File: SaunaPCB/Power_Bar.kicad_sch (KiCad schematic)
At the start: 37 parts, among them J200a1 KL2RM7.62, J200b1 KL3RM7.62, J201a1 KL2RM7.62, J201b1 KL3RM7.62, J202 KL3RM7.62, J203 KL2RM7.62, K200 Relais_SPDT_CO, K201 Relais_SPDT_CO, K202 Relais_SPDT_CO, K203 Relais_SPDT_CO, K204 Relais_SPDT_CO, K205 Relais_SPDT_CO, K206 Relais_SPDT_CO, U1 4N25, U2 4N25, U3 4N25

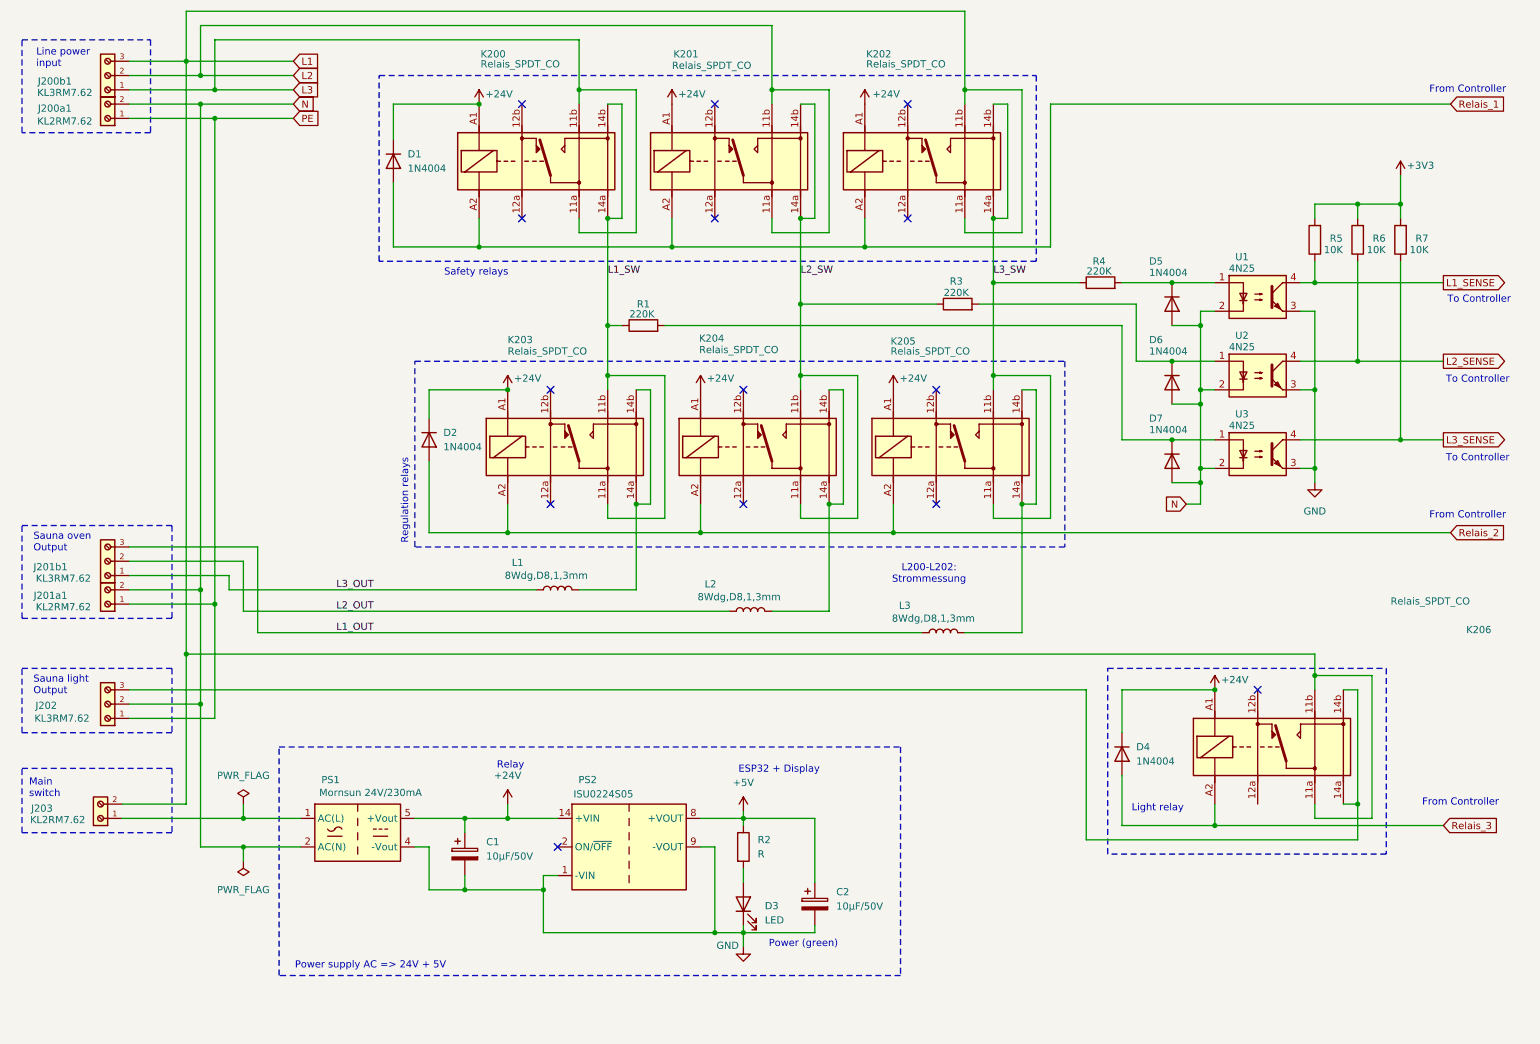
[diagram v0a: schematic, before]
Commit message: Working on schematic and PCB -AC/DC and DC/DC converters with correct symbol and footprint now - rough placement of the power parts
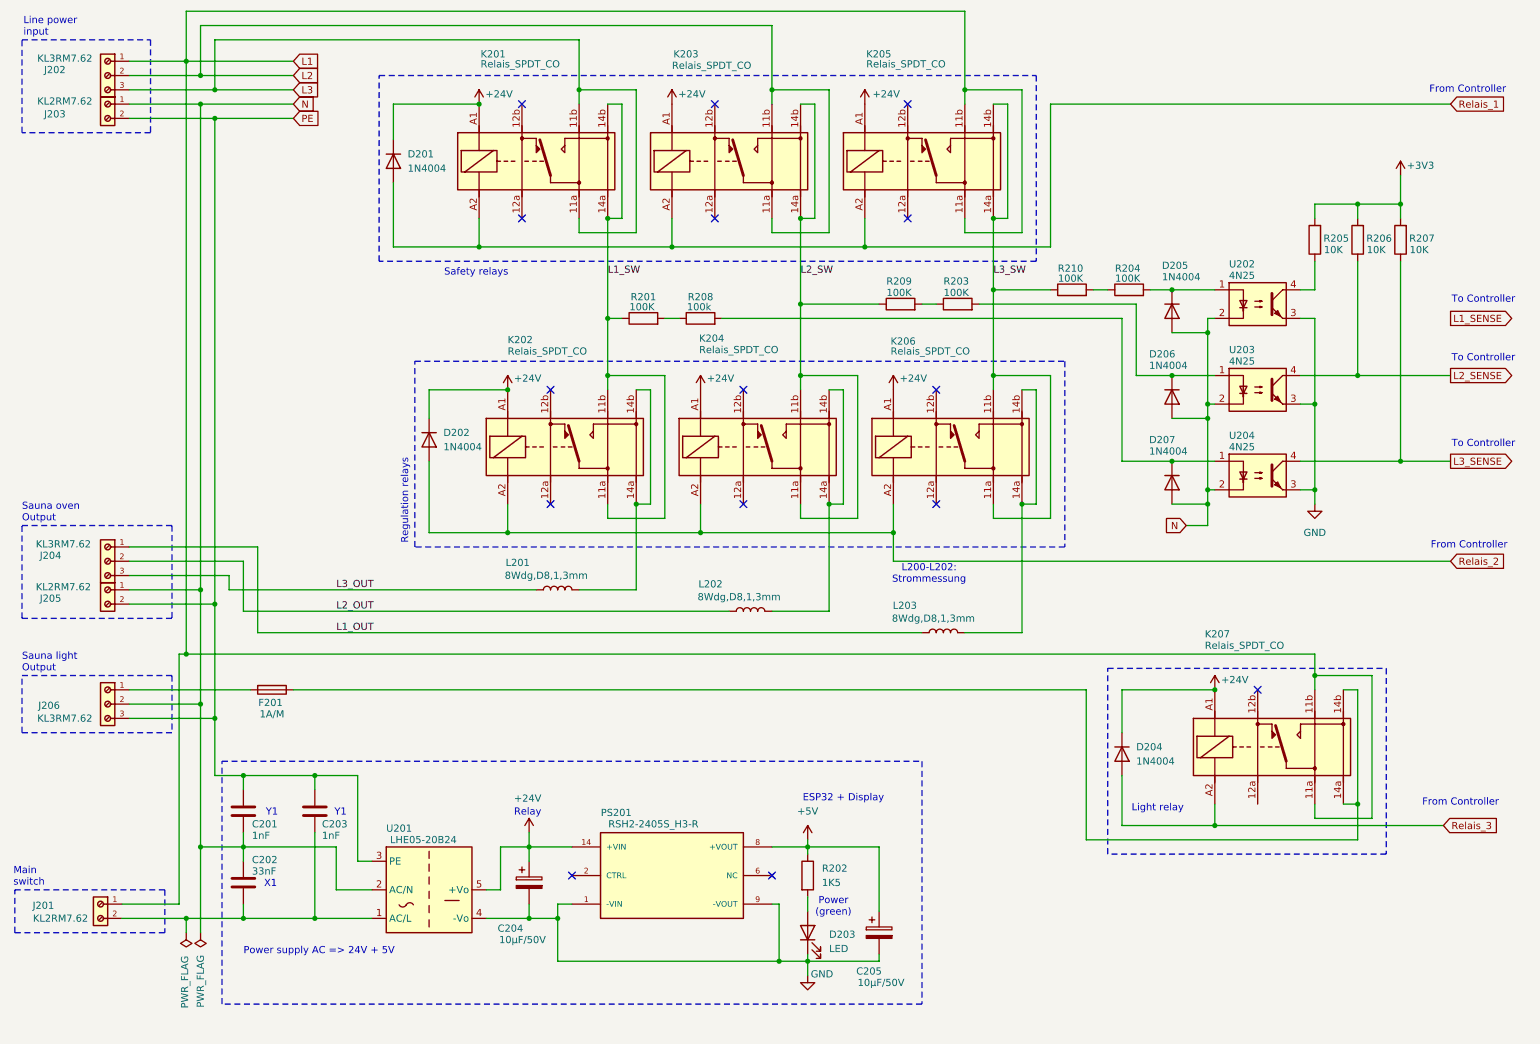
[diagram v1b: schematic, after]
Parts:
- removed PS1: Mornsun 24V/230mA, Converter_ACDC:Converter_ACDC_RECOM_RAC05-xxSK_THT, symbol Converter_ACDC:RAC05-24SK
- removed PS2: ISU0224S05, Converter_DCDC:Converter_DCDC_XP_POWER-ISU02_SMD, symbol Converter_DCDC:ISU0224S05
- added C201, C203: 1nF, Capacitor_THT:C_Axial_L12.0mm_D6.5mm_P15.00mm_Horizontal, symbol Device:C
- added C202: 33nF, Capacitor_THT:C_Axial_L12.0mm_D6.5mm_P15.00mm_Horizontal, symbol Device:C
- added F201: 1A/M, Fuse:Fuseholder_Cylinder-5x20mm_Schurter_0031_8201_Horizontal_Open, symbol Device:Fuse
- added PS201: RSH2-2405S_H3-R, DCDC:CONV_RSH2-2405S_H3-R, symbol DC-DC:RSH2-2405S_H3-R
- added R208: 100k, Resistor_SMD:R_1206_3216Metric, symbol Device:R
- added R209, R210: 100K, Resistor_SMD:R_1206_3216Metric, symbol Device:R
- added U201: LHE05-20B24, Mornsun_ACDC:LHE05-20B24, symbol Project:Mornsun_AC_DC
- D205: renamed from D5; footprint Diode_THT:D_DO-41_SOD81_P10.16mm_Horizontal -> Diode_SMD:D_SMA_Handsoldering
- D206: renamed from D6; footprint Diode_THT:D_DO-41_SOD81_P10.16mm_Horizontal -> Diode_SMD:D_SMA_Handsoldering
- D207: renamed from D7; footprint Diode_THT:D_DO-41_SOD81_P10.16mm_Horizontal -> Diode_SMD:D_SMA_Handsoldering
- L201: renamed from L1; footprint Inductor_THT:L_Toroid_Vertical_L13.0mm_W6.5mm_P5.60mm -> SaunaProject:Current_Coil_15X14
- L202: renamed from L2; footprint Inductor_THT:L_Toroid_Vertical_L13.0mm_W6.5mm_P5.60mm -> SaunaProject:Current_Coil_15X14
- L203: renamed from L3; footprint Inductor_THT:L_Toroid_Vertical_L13.0mm_W6.5mm_P5.60mm -> SaunaProject:Current_Coil_15X14
- R201: renamed from R1; value 220K -> 100K; footprint Resistor_THT:R_Axial_DIN0207_L6.3mm_D2.5mm_P10.16mm_Horizontal -> Resistor_SMD:R_1206_3216Metric
- R202: renamed from R2; value R -> 1K5
- R203: renamed from R3; value 220K -> 100K; footprint Resistor_THT:R_Axial_DIN0207_L6.3mm_D2.5mm_P10.16mm_Horizontal -> Resistor_SMD:R_1206_3216Metric
- R204: renamed from R4; value 220K -> 100K; footprint Resistor_THT:R_Axial_DIN0207_L6.3mm_D2.5mm_P10.16mm_Horizontal -> Resistor_SMD:R_1206_3216Metric
- renumbered C1 to C204, C2 to C205, D1 to D201, D2 to D202, D3 to D203, D4 to D204, J203 to J201, J200b1 to J202, J200a1 to J203, J201b1 to J204, J201a1 to J205, J202 to J206, K200 to K201, K203 to K202, K201 to K203, K202 to K205, K205 to K206, K206 to K207, R5 to R205, R6 to R206, R7 to R207, U1 to U202, U2 to U203, U3 to U204
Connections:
- net +24V: now also PS201.14 (+VIN), U201.5 (+Vo)
- net +5V: now also PS201.8 (+VOUT)
- net GND: now also PS201.1 (-VIN), PS201.9 (-VOUT), U201.4 (-Vo)
- net L1: now also J201.1, J202.1; no longer J201.2, J202.3
- net L1_OUT: now also J204.1; no longer J204.3
- net L1_SENSE: no longer R205.1, U202.4
- net L2_SW: now also R209.1; no longer R203.1
- net L3: now also J202.3; no longer J202.1
- net L3_OUT: now also J204.3; no longer J204.1
- net L3_SW: now also R210.1; no longer R204.1
- net N: now also J203.1, J205.1, C201.2, C202.1, U201.2 (AC/N); no longer J203.2, J205.2
- net PE: now also J203.2, J205.2, J206.3, C201.1, C203.1, U201.3 (PE); no longer J203.1, J205.1, J206.1
- net at D207.1 (K), U204.1: now also R208.2; no longer R201.2
- net at K207.14a, K207.14b: now also F201.1; no longer J206.3
- new net: R201.2, R208.1
- new net: PS201.6 (NC), PS201.7 (NC)
- new net: C202.2, C203.2, J201.2, U201.1 (AC/L)
- new net: R203.1, R209.2
- new net: R205.1, U202.4
- new net: R204.1, R210.2
- new net: F201.2, J206.1
- no-connect marks 14 -> 15
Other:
- note added: "X1"
- note added: "Y1"
- moved on the sheet: C204, C205, D203, D205, D206, D207, J201, R201, R202, R204, U202, U203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

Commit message: Work on documnets and net classes
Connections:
- net K204_Out: now reaches K204.14a, K204.14b, L202.2
- net K206_Out: now reaches K206.14a, K206.14b, L203.2
- net K202_Out: now reaches K202.14a, K202.14b, L201.2
- net Light_Out: now reaches F201.1, K207.14a, K207.14b
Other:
- moved on the sheet: L201, L202, L203
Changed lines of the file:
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@@
 	(text "Power supply AC => 24V + 5V"
 		(exclude_from_sim no)
-		(at 68.072 181.102 0)
+		(at 66.548 188.976 0)
 		(effects
 			(font
@@
 	(wire
 		(pts
-			(xy 43.18 128.27) (xy 43.18 172.72)
+			(xy 44.45 128.27) (xy 44.45 172.72)
 		)
 		(stroke
@@
 	(wire
 		(pts
-			(xy 140.97 120.65) (xy 54.61 120.65)
+			(xy 132.08 120.65) (xy 54.61 120.65)
 		)
 		(stroke
@@
 	(wire
 		(pts
-			(xy 57.15 124.46) (xy 175.26 124.46)
+			(xy 57.15 124.46) (xy 166.37 124.46)
 		)
 		(stroke
@@
 	(wire
 		(pts
-			(xy 52.07 116.84) (xy 106.68 116.84)
+			(xy 52.07 116.84) (xy 90.17 116.84)
 		)
 		(stroke
@@
 	(wire
 		(pts
-			(xy 182.88 124.46) (xy 193.04 124.46)
+			(xy 173.99 124.46) (xy 193.04 124.46)
 		)
 		(stroke
@@
 	(wire
 		(pts
-			(xy 43.18 128.27) (xy 44.45 128.27)
-		)
-		(stroke
-			(width 0)
-			(type default)
-		)
-	)
-	(wire
-		(pts
 			(xy 124.46 81.28) (xy 127 81.28)
 		)
@@
 	(wire
 		(pts
-			(xy 148.59 120.65) (xy 158.75 120.65)
+			(xy 139.7 120.65) (xy 158.75 120.65)
 		)
 		(stroke
@@
 	(wire
 		(pts
-			(xy 114.3 116.84) (xy 124.46 116.84)
+			(xy 97.79 116.84) (xy 124.46 116.84)
 		)
 		(stroke
@@
 	(wire
 		(pts
-			(xy 43.18 172.72) (xy 33.02 172.72)
+			(xy 44.45 172.72) (xy 33.02 172.72)
 		)
 		(stroke
@@
 		)
 	)
+	(label "K202_Out"
+		(at 102.87 116.84 0)
+		(effects
+			(font
+				(size 1.27 1.27)
+			)
+			(justify left bottom)
+		)
+	)
 	(label "L3_OUT"
 		(at 71.12 116.84 0)
@@
 		)
 	)
+	(label "Light_Out"
+		(at 71.12 134.62 0)
+		(effects
+			(font
+				(size 1.27 1.27)
+			)
+			(justify left bottom)
+		)
+	)
 	(label "L3_SW"
 		(at 187.96 60.96 0)
@@
 		)
 	)
+	(label "K206_Out"
+		(at 177.8 124.46 0)
+		(effects
+			(font
+				(size 1.27 1.27)
+			)
+			(justify left bottom)
+		)
+	)
+	(label "K204_Out"
+		(at 144.78 120.65 0)
+		(effects
+			(font
+				(size 1.27 1.27)
+			)
+			(justify left bottom)
+		)
+	)
 	(global_label "L2_SENSE"
 		(shape output)
@@
 	(symbol
 		(lib_id "Device:L")
-		(at 144.78 120.65 90)
+		(at 135.89 120.65 90)
 		(unit 1)
 		(exclude_from_sim no)
@@
 		(dnp no)
 		(property "Reference" "L202"
-			(at 137.668 115.824 90)
+			(at 128.778 115.824 90)
 			(effects
 				(font
@@
 		)
 		(property "Value" "8Wdg,D8,1,3mm"
-			(at 142.748 118.11 90)
+			(at 133.858 118.11 90)
 			(effects
 				(font
@@
 		)
 		(property "Footprint" "SaunaProject:Current_Coil_15X14"
-			(at 144.78 120.65 0)
+			(at 135.89 120.65 0)
 			(effects
 				(font
@@
 		)
 		(property "Datasheet" "~"
-			(at 144.78 120.65 0)
+			(at 135.89 120.65 0)
 			(effects
 				(font
@@
 		)
 		(property "Description" "Inductor"
-			(at 144.78 120.65 0)
+			(at 135.89 120.65 0)
 			(effects
 				(font
@@
 	(symbol
 		(lib_id "Device:L")
-		(at 179.07 124.46 90)
+		(at 170.18 124.46 90)
 		(unit 1)
 		(exclude_from_sim no)
@@
 		(dnp no)
 		(property "Reference" "L203"
-			(at 172.212 119.634 90)
+			(at 163.322 119.634 90)
 			(effects
 				(font
@@
 		)
 		(property "Value" "8Wdg,D8,1,3mm"
-			(at 177.292 121.92 90)
+			(at 168.402 121.92 90)
 			(effects
 				(font
@@
 		)
 		(property "Footprint" "SaunaProject:Current_Coil_15X14"
-			(at 179.07 124.46 0)
+			(at 170.18 124.46 0)
 			(effects
 				(font
@@
 		)
 		(property "Datasheet" "~"
-			(at 179.07 124.46 0)
+			(at 170.18 124.46 0)
 			(effects
 				(font
@@
 		)
 		(property "Description" "Inductor"
-			(at 179.07 124.46 0)
+			(at 170.18 124.46 0)
 			(effects
 				(font
@@
 	(symbol
 		(lib_id "Device:L")
-		(at 110.49 116.84 90)
+		(at 93.98 116.84 90)
 		(unit 1)
 		(exclude_from_sim no)
@@
 		(dnp no)
 		(property "Reference" "L201"
-			(at 103.378 112.014 90)
+			(at 86.868 112.014 90)
 			(effects
 				(font
@@
 		)
 		(property "Value" "8Wdg,D8,1,3mm"
-			(at 108.458 114.3 90)
+			(at 91.948 114.3 90)
 			(effects
 				(font
@@
 		)
 		(property "Footprint" "SaunaProject:Current_Coil_15X14"
-			(at 110.49 116.84 0)
+			(at 93.98 116.84 0)
 			(effects
 				(font
@@
 		)
 		(property "Datasheet" "~"
-			(at 110.49 116.84 0)
+			(at 93.98 116.84 0)
 			(effects
 				(font
@@
 		)
 		(property "Description" "Inductor"
-			(at 110.49 116.84 0)
+			(at 93.98 116.84 0)
 			(effects
 				(font

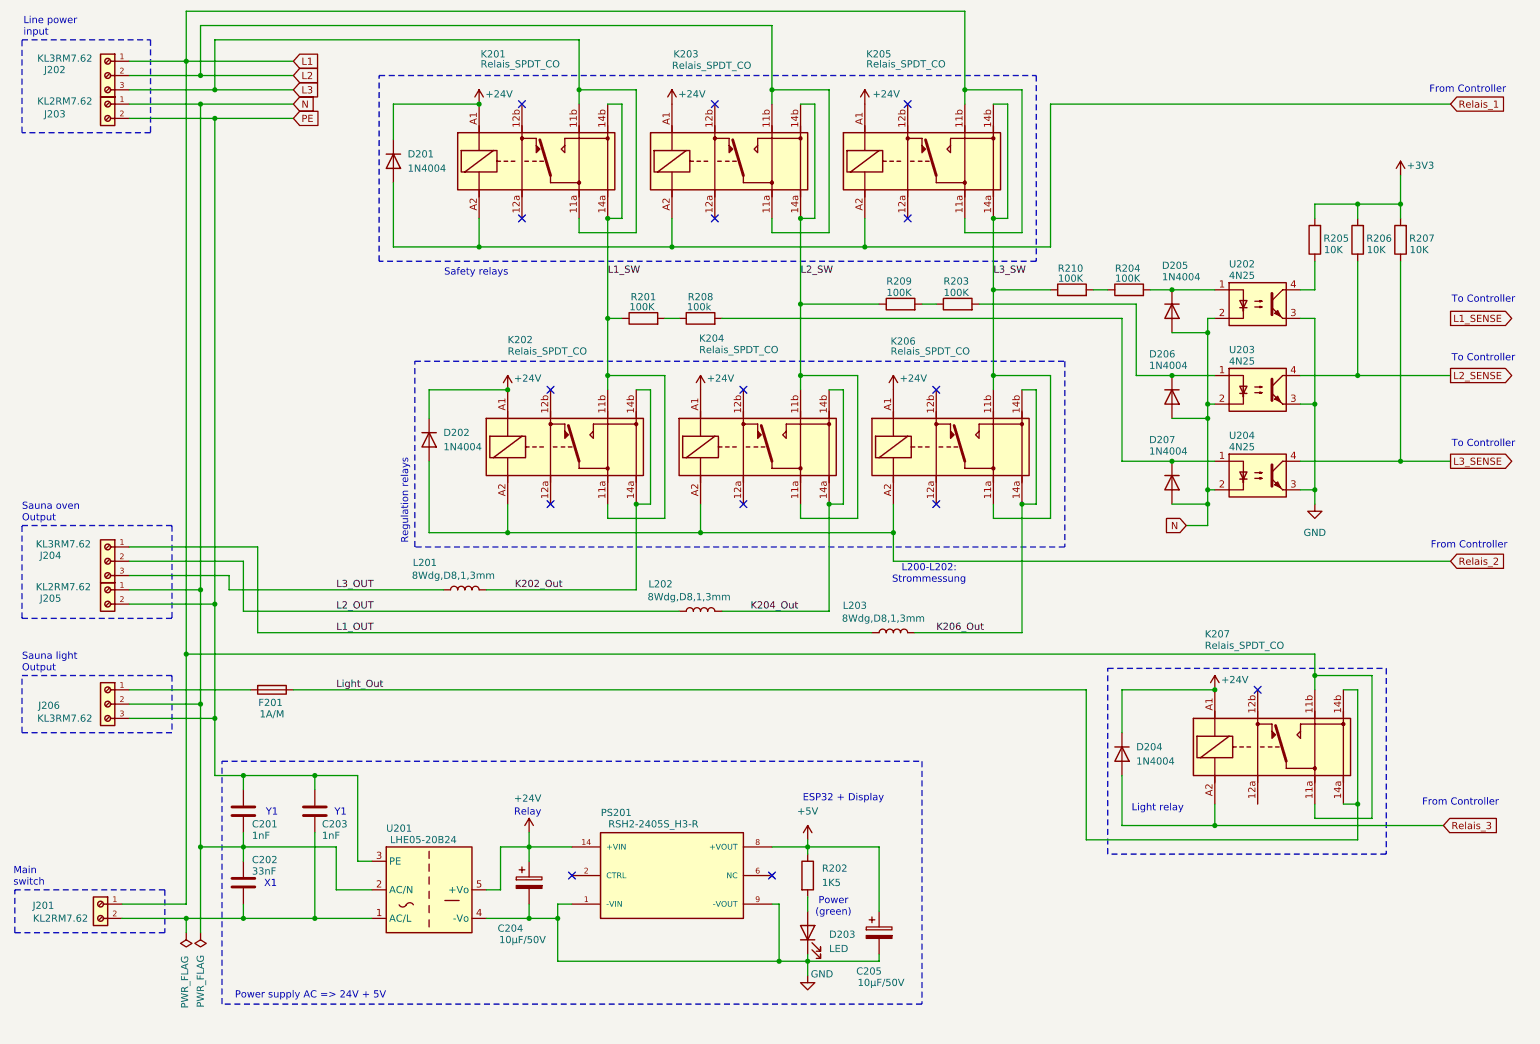
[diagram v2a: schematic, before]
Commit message: Working on PCB placment optimisation Trace width and distance
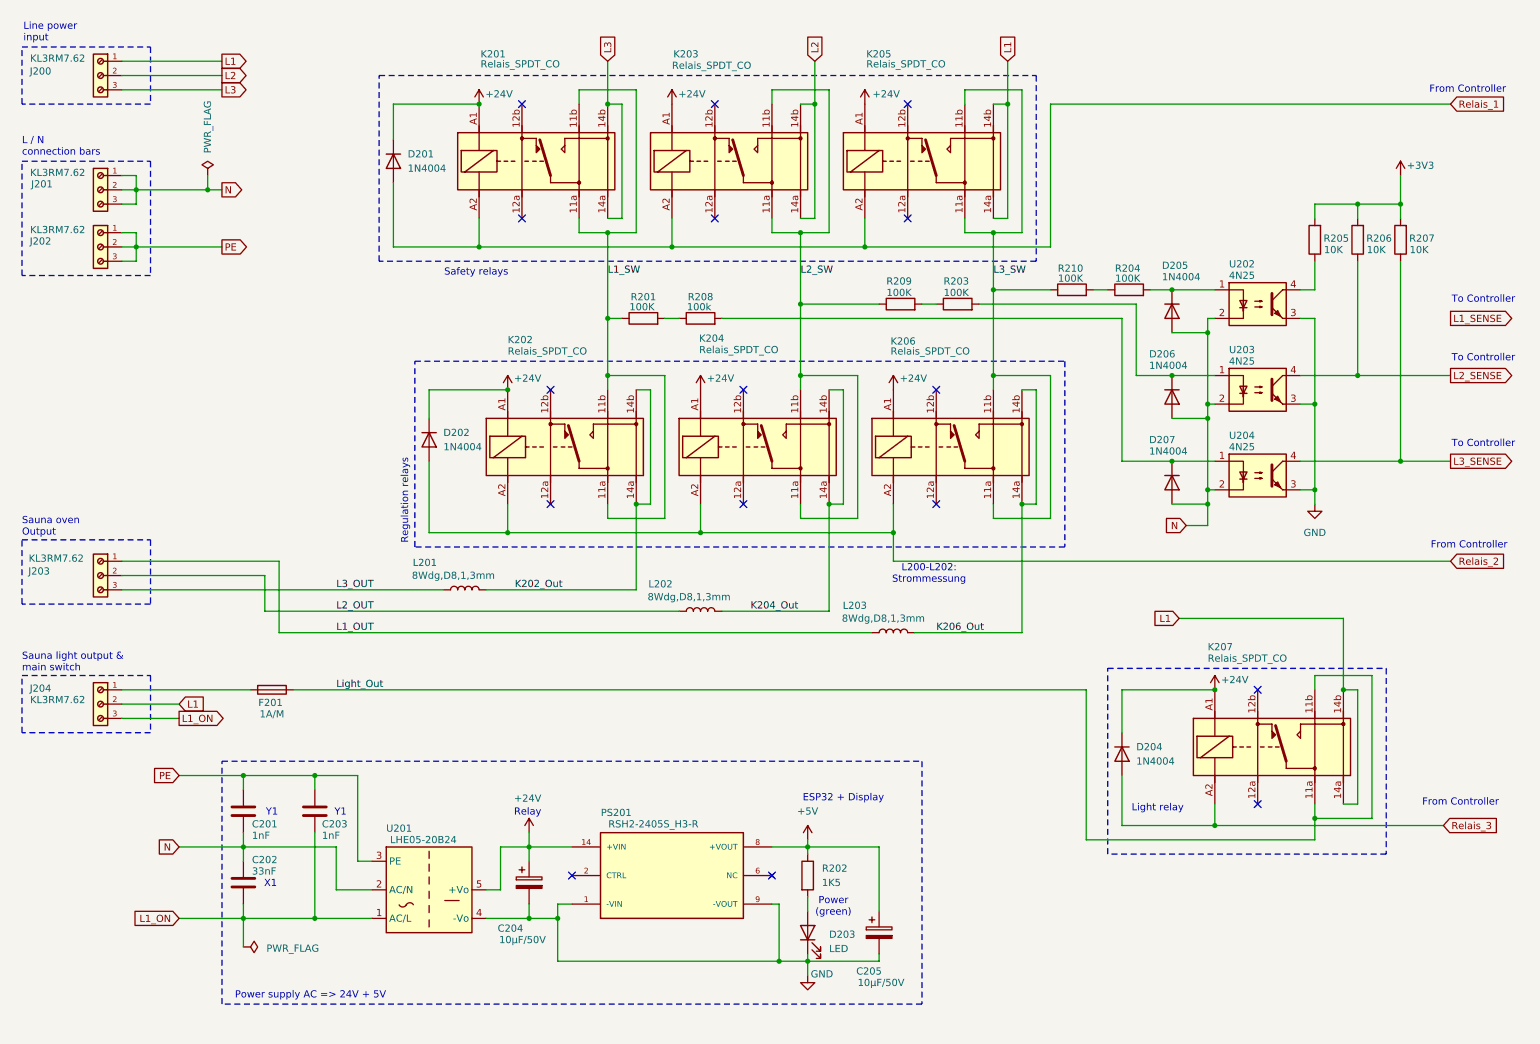
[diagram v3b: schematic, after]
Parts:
- removed J201, J203, J205: KL2RM7.62, MyConnectors:Terminal_Block_2_RM7.62, symbol MyConnectors:Terminal_Block_2
- added J201, J202: KL3RM7.62, MyConnectors:Terminal_Block_3_RM7.62, symbol MyConnectors:Terminal_Block_3
- renumbered J202 to J200, J204 to J203, J206 to J204
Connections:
- net L1: now also J204.2, K205.14a, K205.14b, K207.14a, K207.14b; no longer K205.11a, K205.11b, K207.11a, K207.11b
- net L1_SW: now also K201.11a, K201.11b; no longer K201.14a, K201.14b
- net L2: now also K203.14a, K203.14b; no longer K203.11a, K203.11b
- net L2_SW: now also K203.11a, K203.11b; no longer K203.14a, K203.14b
- net L3: now also K201.14a, K201.14b; no longer K201.11a, K201.11b
- net L3_SW: now also K205.11a, K205.11b; no longer K205.14a, K205.14b
- net Light_Out: now also K207.11a, K207.11b; no longer K207.14a, K207.14b
- net N: now also J201.1, J201.2, J201.3; no longer J204.2
- net PE: now also J202.1, J202.2, J202.3; no longer J204.3
- net L1_ON: now reaches C202.2, C203.2, U201.1 (AC/L)
- net L1_ON: now also J204.3
- no-connect marks 15 -> 16
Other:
- note added: "L / N connection bars"
- note added: "Sauna light output & main switch"
- note removed: "Main switch"
- note removed: "Sauna light Output"
- moved on the sheet: J200, J203, J204
